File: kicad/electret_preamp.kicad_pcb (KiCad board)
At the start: 2 copper layers, 34 x 20.5 mm, 15 parts, among them U1 NE5532

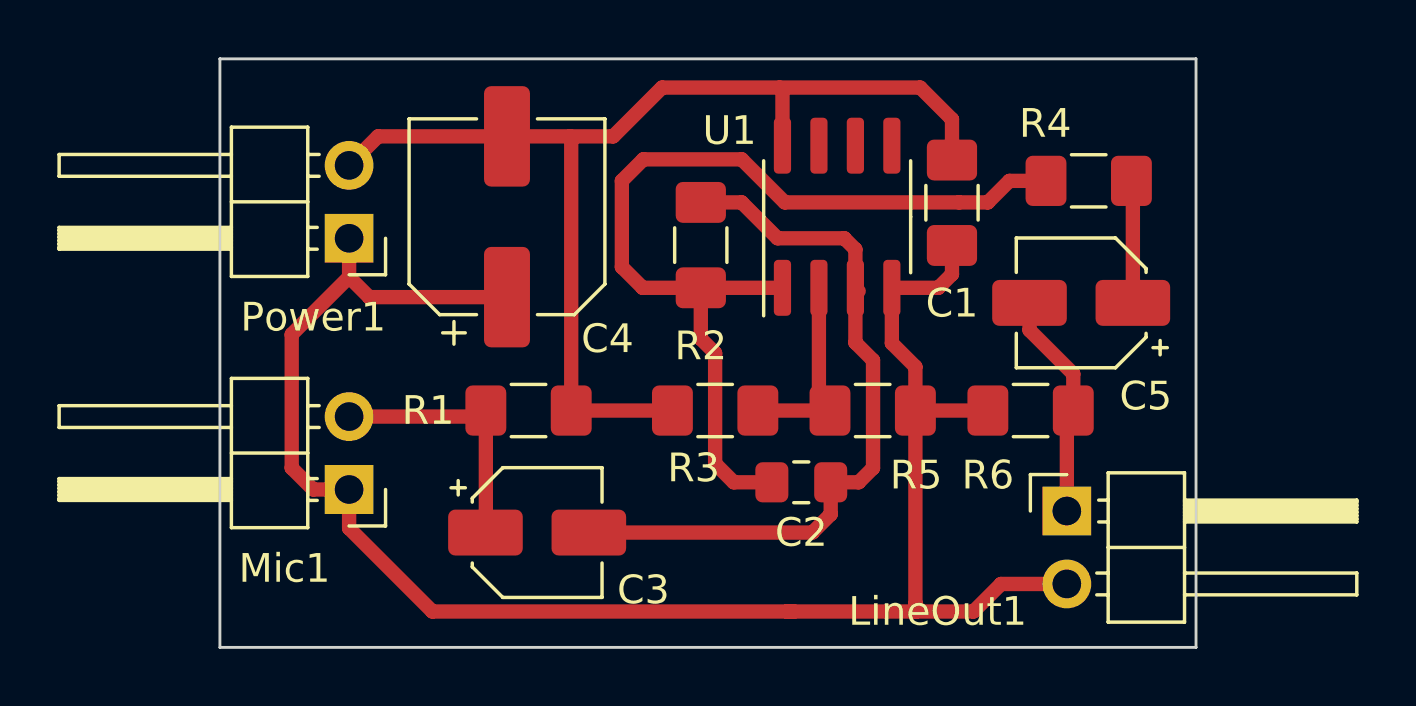
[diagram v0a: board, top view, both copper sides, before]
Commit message: Fix errors in KiCAD files
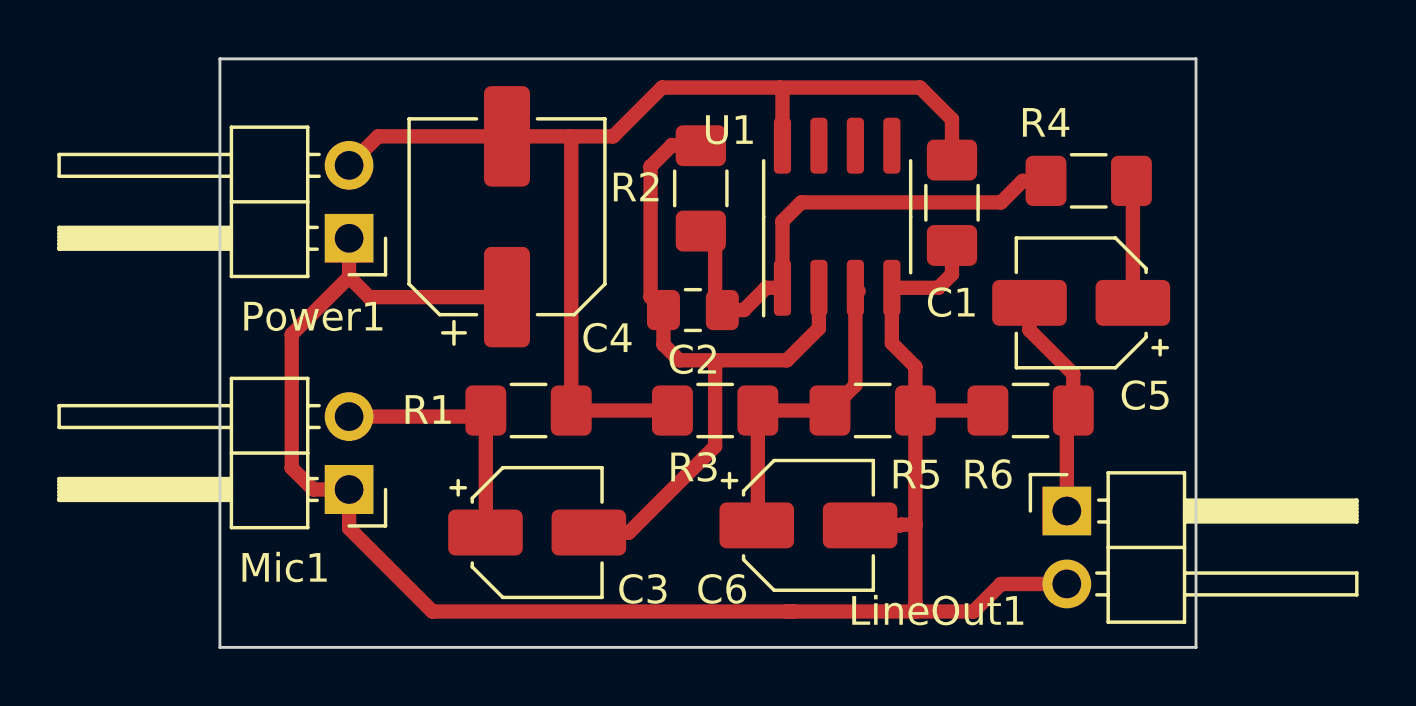
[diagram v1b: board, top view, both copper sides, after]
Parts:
- added C6: 10u, Capacitor_SMD:CP_Elec_4x5.8, F.Cu at (131.5, 74.5)
- Mic1: value Microphone_Condenser -> MK100
- moved C2 7.09 mm to (127.5, 67.0), turned to 180 degrees
- moved R2 1.97 mm to (127.8, 62.8)
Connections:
- U1 pad 2: Net-(C6-Pad1) -> Net-(C2-Pad2)
- U1 pad 3: Net-(C2-Pad2) -> Net-(C6-Pad1)
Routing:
- net Net-(C2-Pad1): track 33.5 -> 17.6 mm
- net Net-(C6-Pad1): track 6.95 -> 11.3 mm
- net GND: track 62.6 -> 64.5 mm
- net Net-(C2-Pad2): track 25.6 -> 24.6 mm

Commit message: Polarized cap in wrong direction
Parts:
- R2: value 270k -> 180k
- turned C4 to 270 degrees
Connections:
- C4 pad 1: GND -> +5V
- C4 pad 2: +5V -> GND
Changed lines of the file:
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@@
       (effects (font (size 1 1) (thickness 0.15)))
     )
-    (fp_text value 270k (at 3.4875 0 180) (layer F.Fab)
+    (fp_text value 180k (at 3.4875 0 180) (layer F.Fab)
       (effects (font (size 1 1) (thickness 0.15)))
     )
@@
   )
   (module Capacitor_SMD:CP_Elec_6.3x9.9 (layer F.Cu)
-    (at 121 63.75 90)
+    (at 121 63.75 270)
     (descr "SMD capacitor, aluminum electrolytic, Panasonic C10, 6.3x9.9mm")
     (tags "capacitor electrolytic")
@@
     (fp_line (start 3.3 -3.3) (end 3.3 3.3) (layer F.Fab) (width 0.1))
     (fp_circle (center 0 0) (end 3.15 0) (layer F.Fab) (width 0.1))
-    (pad 2 smd roundrect (at 2.8 0 90) (size 3.5 1.6) (layers F.Cu F.Paste F.Mask) (roundrect_rratio 0.15625)
+    (pad 2 smd roundrect (at 2.8 0 270) (size 3.5 1.6) (layers F.Cu F.Paste F.Mask) (roundrect_rratio 0.15625)
+      (net 2 GND))
+    (pad 1 smd roundrect (at -2.8 0 270) (size 3.5 1.6) (layers F.Cu F.Paste F.Mask) (roundrect_rratio 0.15625)
       (net 1 +5V))
-    (pad 1 smd roundrect (at -2.8 0 90) (size 3.5 1.6) (layers F.Cu F.Paste F.Mask) (roundrect_rratio 0.15625)
-      (net 2 GND))
     (model ${KISYS3DMOD}/Capacitor_SMD.3dshapes/CP_Elec_6.3x9.9.wrl
       (at (xyz 0 0 0))
@@
   (segment (start 139.775 62.5) (end 138.9625 62.5) (width 0.5) (layer F.Cu) (net 4))
   (segment (start 138.9625 62.5) (end 138.2125 63.25) (width 0.5) (layer F.Cu) (net 4))
-  (segment (start 133.25 66.34) (end 133.135 66.225) (width 0.5) (layer F.Cu) (net 8) (status 30))
   (segment (start 120.0525 70.71) (end 120.2625 70.5) (width 0.5) (layer F.Cu) (net 5) (status 30))
   (segment (start 115.5 70.71) (end 120.0525 70.71) (width 0.5) (layer F.Cu) (net 5) (status 30))
@@
   (segment (start 142.8 62.55) (end 142.75 62.5) (width 0.5) (layer F.Cu) (net 7))
   (segment (start 142.8 66.75) (end 142.8 62.55) (width 0.5) (layer F.Cu) (net 7))
+  (segment (start 133.25 66.34) (end 133.135 66.225) (width 0.5) (layer F.Cu) (net 8) (status 30))
   (segment (start 129.7375 70.5) (end 132.25 70.5) (width 0.5) (layer F.Cu) (net 8) (status 30))
   (segment (start 133.135 69.615) (end 132.25 70.5) (width 0.5) (layer F.Cu) (net 8))

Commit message: Some layout fixes
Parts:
- moved C4 0.50 mm to (121.5, 63.8)
- moved C3 0.25 mm to (122.0, 74.5)
- moved C5 0.25 mm to (141.0, 66.5)
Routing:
- net GND: track 64.5 -> 65.5 mm
